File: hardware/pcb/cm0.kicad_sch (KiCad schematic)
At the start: 19 parts, among them Q201 2N7002, Q202 2N7002, U201 CM0100008, U202 SN74LVC1G125DBV

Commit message: Use power symbols for the CM0 3.3V and 1.8V rails
Rename CM0_3V3 to +3V3_CM0 and CM0_1V8 to +1V8_CM0, replace their
labels on the cm0, display and peripherals sheets with power symbols,
and update the docs to match.

Co-Authored-By: Claude Opus 5.5 <noreply@anthropic.com>
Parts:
- TP201: value CM0_3V3 -> +3V3_CM0
- TP202: value CM0_1V8 -> +1V8_CM0
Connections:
- net CM0_1V8 renamed +1V8_CM0
- net CM0_3V3 renamed +3V3_CM0
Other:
- note added: "UART の受信バッファ（+3V3_CM0 で動作）"
- note removed: "UART の受信バッファ（CM0_3V3 で動作）"

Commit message: Assign 0603 parts, use 30k for ILM, and switch the LDO to AP2127
Give every resistor and capacitor a 0603 footprint and an LCSC number
(Basic where possible), change the ILM resistor to a 30k Basic part,
and replace the XC6206 with an AP2127N-3.3 from stock. Record the
decisions and drop the resolved open items.

Co-Authored-By: Claude Opus 5.5 <noreply@anthropic.com>
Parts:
- C201: footprint (none) -> Capacitor_SMD:C_0603_1608Metric; LCSC (none) -> C96446
- C202, C203: footprint (none) -> Capacitor_SMD:C_0603_1608Metric; LCSC (none) -> C14663
- R201: footprint (none) -> Resistor_SMD:R_0603_1608Metric; LCSC (none) -> C25804
- R202: footprint (none) -> Resistor_SMD:R_0603_1608Metric; LCSC (none) -> C25803
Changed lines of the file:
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@@
 			)
 		)
-		(property "Footprint" ""
+		(property "Footprint" "Capacitor_SMD:C_0603_1608Metric"
 			(at 39.0652 100.33 0)
 			(hide yes)
@@
 			)
 		)
+		(property "LCSC" "C96446"
+			(at 38.1 96.52 0)
+			(show_name no)
+			(do_not_autoplace no)
+			(hide yes)
+			(effects
+				(font
+					(size 1.27 1.27)
+				)
+			)
+		)
 		(property "Datasheet" ""
 			(at 38.1 96.52 0)
@@
 			)
 		)
-		(property "Footprint" ""
+		(property "Footprint" "Capacitor_SMD:C_0603_1608Metric"
 			(at 336.2452 77.47 0)
 			(hide yes)
@@
 			)
 		)
+		(property "LCSC" "C14663"
+			(at 335.28 73.66 0)
+			(show_name no)
+			(do_not_autoplace no)
+			(hide yes)
+			(effects
+				(font
+					(size 1.27 1.27)
+				)
+			)
+		)
 		(property "Datasheet" ""
 			(at 335.28 73.66 0)
@@
 			)
 		)
-		(property "Footprint" ""
+		(property "Footprint" "Resistor_SMD:R_0603_1608Metric"
 			(at 120.142 228.6 0)
 			(hide yes)
@@
 			)
 		)
+		(property "LCSC" "C25803"
+			(at 121.92 228.6 0)
+			(show_name no)
+			(do_not_autoplace no)
+			(hide yes)
+			(effects
+				(font
+					(size 1.27 1.27)
+				)
+			)
+		)
 		(property "Datasheet" ""
 			(at 121.92 228.6 0)
@@
 			)
 		)
-		(property "Footprint" ""
+		(property "Footprint" "Capacitor_SMD:C_0603_1608Metric"
 			(at 49.2252 100.33 0)
 			(hide yes)
@@
 			)
 		)
+		(property "LCSC" "C14663"
+			(at 48.26 96.52 0)
+			(show_name no)
+			(do_not_autoplace no)
+			(hide yes)
+			(effects
+				(font
+					(size 1.27 1.27)
+				)
+			)
+		)
 		(property "Datasheet" ""
 			(at 48.26 96.52 0)
@@
 			)
 		)
-		(property "Footprint" ""
+		(property "Footprint" "Resistor_SMD:R_0603_1608Metric"
 			(at 120.142 175.26 0)
 			(hide yes)
@@
 			(effects
 				(font
+					(size 1.27 1.27)
+				)
+			)
+		)
+		(property "LCSC" "C25804"
+			(at 121.92 175.26 0)
+			(show_name no)
+			(do_not_autoplace no)
+			(hide yes)
+			(effects
+				(font

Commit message: Add audio, microSD and keyboard I2C, and place parts on the PCB
Schematics:
- Swap the MAX98357A for the TLV320DAC3100 (headphone and speaker out).
  A 12 MHz oscillator drives MCLK and the codec is the I2S clock master,
  so the stock simple-audio-card works without a custom machine driver.
- Add the microSD slot for the CM0Lite; the SD pull-ups are footprints only.
- Add HID over I2C from the RP2040 to the CM0 (KB_SDA/KB_SCL/KB_INT) on
  i2c-gpio, so the keyboard works on stock Raspberry Pi OS. Add test pads.
- Use power symbols for +1V1, assign footprints and LCSC numbers, and
  fix global label shapes.

PCB: 228.6 x 146.2 mm outline and a provisional bottom-side placement,
with HID USB top-left and Linux USB top-right. Add footprints for the CM0,
TPS2121 (RUX), the 22-pin DSI FPC and the CR2032 holder.

Docs: record the decisions and open items. Add a draft device tree
overlay for the audio codec.

Co-Authored-By: Claude Opus 5.5 <noreply@anthropic.com>
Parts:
- added C204: 100n, Capacitor_SMD:C_0603_1608Metric, symbol Device:C
- added C205: 10u, Capacitor_SMD:C_0603_1608Metric, symbol Device:C
- added J201: microSD, Connector_Card:microSD_HC_Hirose_DM3AT-SF-PEJM5, symbol Connector:Micro_SD_Card_Det_Hirose_DM3AT
- added R203, R204, R205, R206, R207: 100k, Resistor_SMD:R_0603_1608Metric, symbol Device:R
- added R208, R209: 4.7k, Resistor_SMD:R_0603_1608Metric, symbol Device:R
- added R210: 10k, Resistor_SMD:R_0603_1608Metric, symbol Device:R
- TP201, TP202, TP203, TP204, TP205, TP206, TP207, TP208, TP209, TP210: footprint (none) -> TestPoint:TestPoint_Pad_D1.5mm
- U201: value CM0100008 -> CM0100000; footprint (none) -> Skjar:RaspberryPi_CM0_Castellated; LCSC C52108791 -> (none); LCSC_1 C52108791 -> (none); MPN CM0100008 -> CM0100000
- U201: value CM0100008 -> CM0100000; footprint (none) -> Skjar:RaspberryPi_CM0_Castellated; LCSC C52108791 -> (none); MPN CM0100008 -> CM0100000
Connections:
- net +3V3_CM0: now also C204.1, C205.1, J201.4 (VDD), R203.1, R204.1, R205.1, R206.1, R207.1, R208.1, R209.1, R210.1
- net GND: now also C204.2, C205.2, J201.6 (VSS), J201.SH (SHIELD)
- net KB_SDA: now reaches U201.101 (GPIO23)
- net KB_SDA: now also R208.2
- net HP_DET: now reaches U201.107 (GPIO17)
- net KB_INT: now reaches U201.94 (GPIO25)
- net KB_INT: now also R210.2
- net KB_SCL: now reaches U201.98 (GPIO24)
- net KB_SCL: now also R209.2
- net SD_DAT1: now reaches U201.124 (SD_DAT1)
- net SD_DAT1: now also J201.8 (DAT1), R205.2
- net SD_DAT0: now reaches U201.125 (SD_DAT0)
- net SD_DAT0: now also J201.7 (DAT0), R204.2
- net SD_CLK: now reaches U201.127 (SD_CLK)
- net SD_CLK: now also J201.5 (CLK)
- net SD_CMD: now reaches U201.128 (SD_CMD)
- net SD_CMD: now also J201.3 (CMD), R203.2
- net SD_DAT3: now reaches U201.130 (SD_DAT3)
- net SD_DAT3: now also J201.2 (DAT3/CD), R207.2
- net SD_DAT2: now reaches U201.131 (SD_DAT2)
- net SD_DAT2: now also J201.1 (DAT2), R206.2
- net AMP_SD renamed CODEC_RST
- no-connect marks 51 -> 43
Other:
- note removed: "シート外へ"
- moved on the sheet: C201, C202, Q201, Q202, R201, R202, U201A, U201D, U202

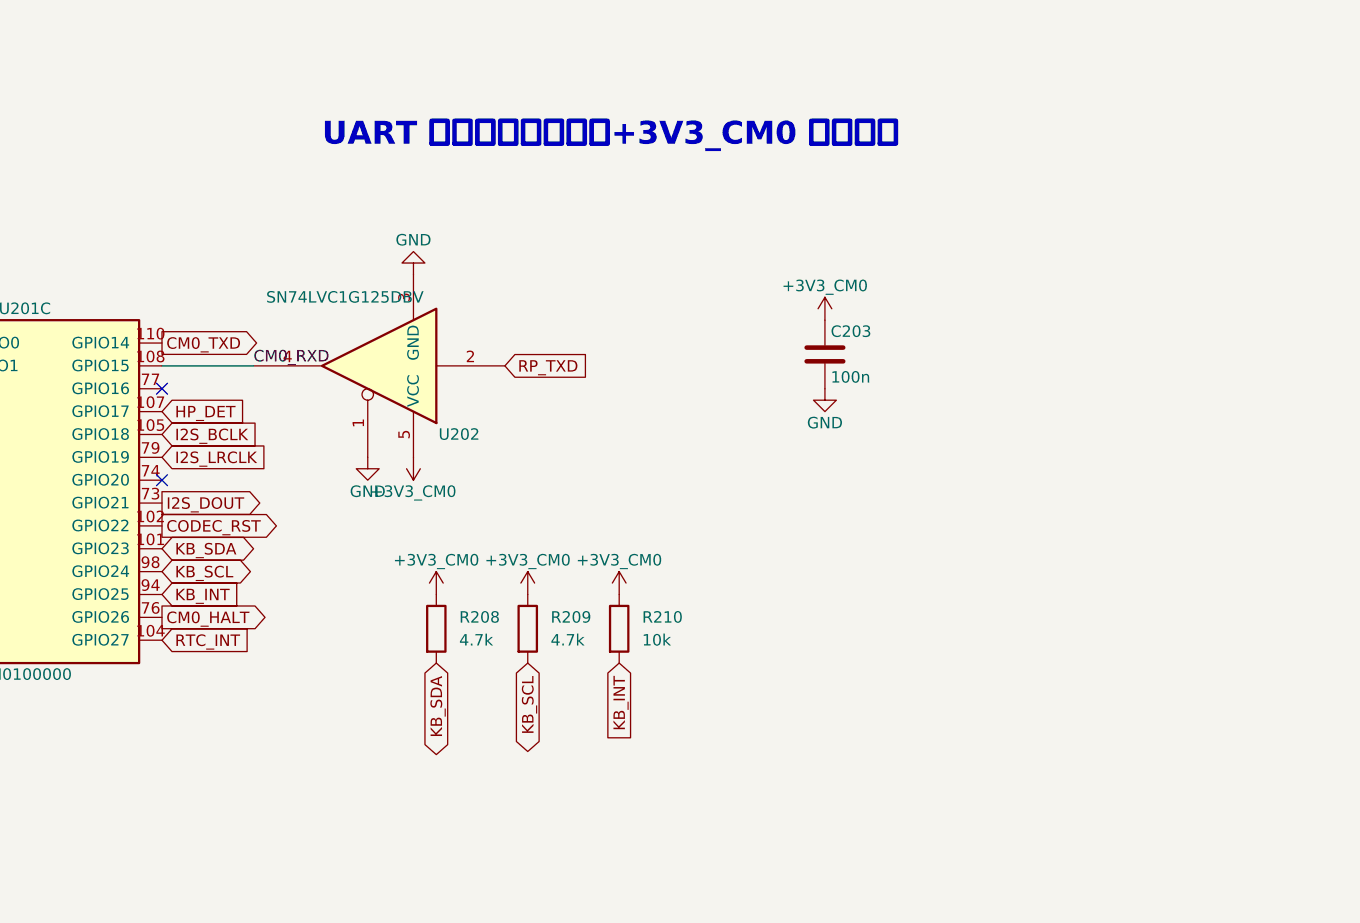
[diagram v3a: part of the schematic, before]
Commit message: Add per-key RGB, finish schematic wiring, and document HID over I2C
- Add SK6812MINI-E per-key RGB with a switched +5V_LED rail and an
  AHCT buffer on the data line; remove SW102 to free GPIO20
- Use D_Small for the matrix diodes and replace labels with wires
- Tidy the keymatrix sheet layout without changing connectivity
- Document the HID over I2C keyboard path, back-power rules and
  role split across README and docs

Co-Authored-By: Claude Opus 5.5 <noreply@anthropic.com>
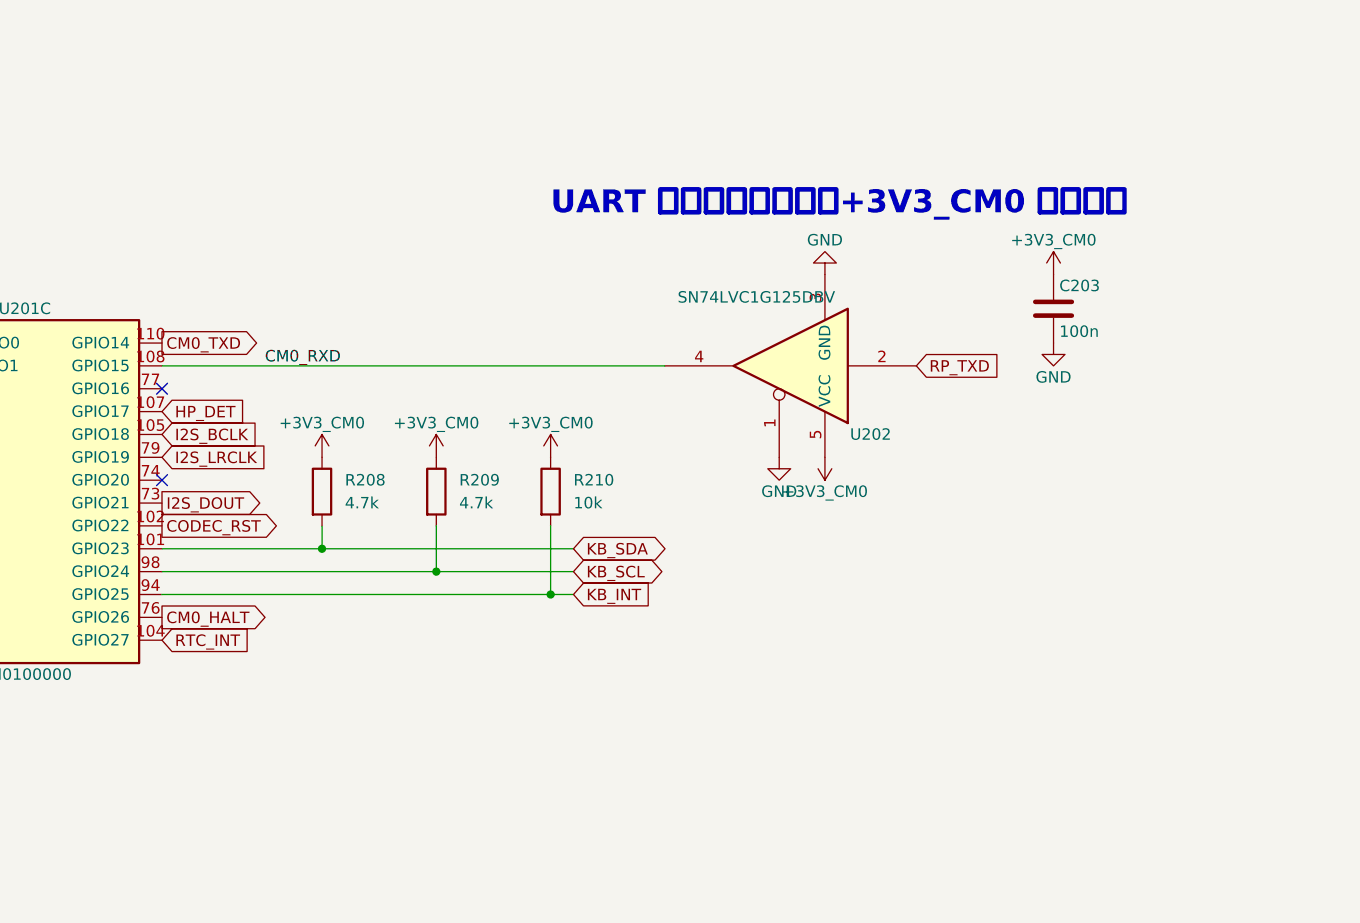
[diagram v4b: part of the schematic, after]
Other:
- moved on the sheet: C203, R208, R209, R210, U202
